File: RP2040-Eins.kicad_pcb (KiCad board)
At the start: 2 copper layers, 45 parts, among them J1 Barrel_Jack_Switch, J2 CONN_ICSP, J5 CONN_R3, J6 USB_B_Micro, J7 CONN_JTAG, Q1 AO3401A, SW1 BOOTSEL, SW2 RESET, U1 W25Q128JVS, U2 RP2040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

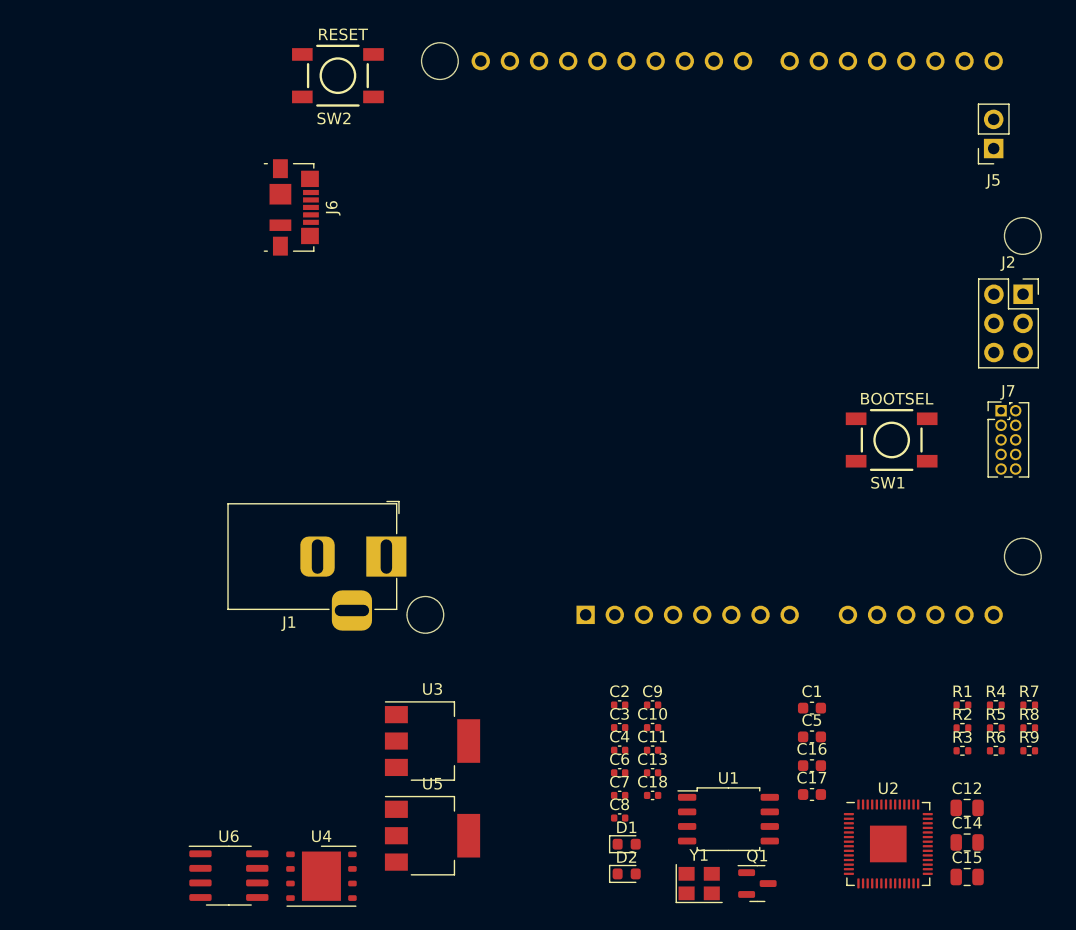
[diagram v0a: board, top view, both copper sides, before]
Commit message: Added board edge
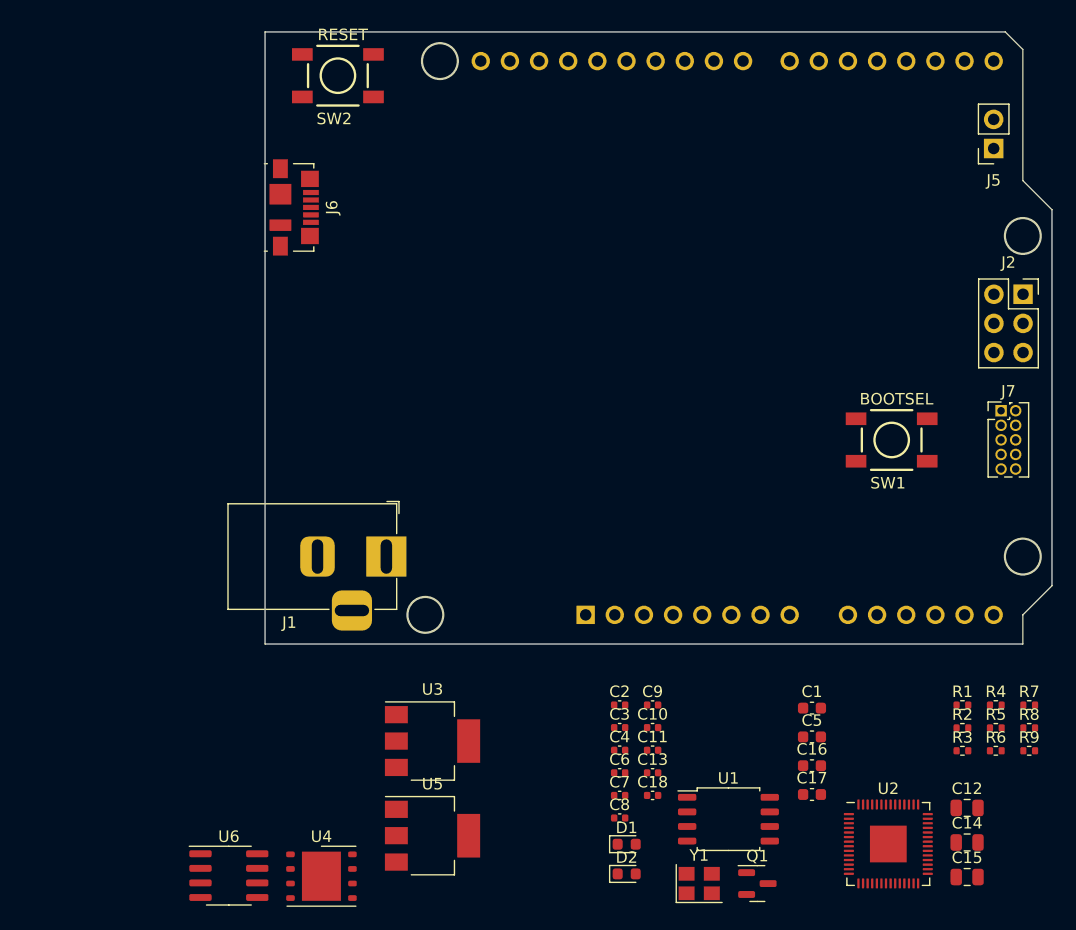
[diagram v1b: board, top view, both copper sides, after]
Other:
- board outline added: 68.6 x 53.3 mm
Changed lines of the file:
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@@
     )
   )
+  (gr_line (start 127 73.66) (end 191.516 73.66)
+    (stroke (width 0.1) (type default)) (layer "Edge.Cuts"))
+  (gr_line (start 193.04 75.184) (end 193.04 86.614)
+    (stroke (width 0.1) (type default)) (layer "Edge.Cuts"))
+  (gr_line (start 195.58 121.92) (end 193.04 124.46)
+    (stroke (width 0.1) (type default)) (layer "Edge.Cuts"))
+  (gr_line (start 191.516 73.66) (end 193.04 75.184)
+    (stroke (width 0.1) (type default)) (layer "Edge.Cuts"))
+  (gr_line (start 193.04 127) (end 127 127)
+    (stroke (width 0.1) (type default)) (layer "Edge.Cuts"))
+  (gr_line (start 193.04 86.614) (end 195.58 89.154)
+    (stroke (width 0.1) (type default)) (layer "Edge.Cuts"))
+  (gr_line (start 193.04 124.46) (end 193.04 127)
+    (stroke (width 0.1) (type default)) (layer "Edge.Cuts"))
+  (gr_circle (center 193.04 91.44) (end 193.04 89.916)
+    (stroke (width 0.1) (type default)) (fill none) (layer "Edge.Cuts"))
+  (gr_circle (center 193.04 119.38) (end 193.04 117.856)
+    (stroke (width 0.1) (type default)) (fill none) (layer "Edge.Cuts"))
+  (gr_line (start 127 127) (end 127 73.66)
+    (stroke (width 0.1) (type default)) (layer "Edge.Cuts"))
+  (gr_circle (center 142.24 76.2) (end 142.24 74.676)
+    (stroke (width 0.1) (type default)) (fill none) (layer "Edge.Cuts"))
+  (gr_line (start 195.58 89.154) (end 195.58 121.92)
+    (stroke (width 0.1) (type default)) (layer "Edge.Cuts"))
+  (gr_circle (center 140.97 124.46) (end 140.97 122.936)
+    (stroke (width 0.1) (type default)) (fill none) (layer "Edge.Cuts"))
 )

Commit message: Exchanged Arduino board shape with separate connectors
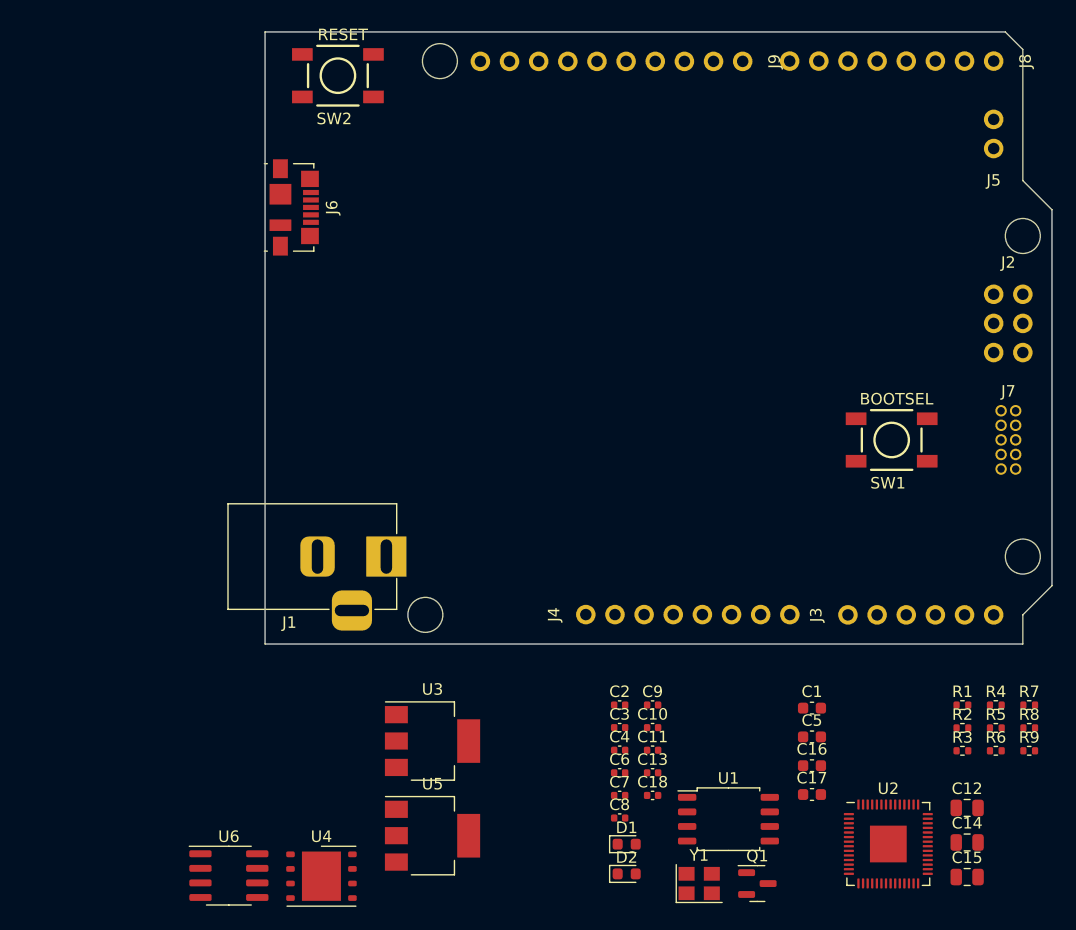
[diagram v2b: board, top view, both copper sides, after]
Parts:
- removed A1: Arduino_UNO_R3, Module:Arduino_UNO_R3_WithMountingHoles
- added J3: CONN_A, Connector_PinSocket_2.54mm:PinSocket_1x06_P2.54mm_Vertical, F.Cu at (177.8, 124.5)
- added J4: CONN_P, Connector_PinSocket_2.54mm:PinSocket_1x08_P2.54mm_Vertical, F.Cu at (155.0, 124.4)
- added J8: CONN_D1, Connector_PinSocket_2.54mm:PinSocket_1x08_P2.54mm_Vertical, F.Cu at (190.5, 76.2)
- added J9: CONN_D2, Connector_PinSocket_2.54mm:PinSocket_1x10_P2.54mm_Vertical, F.Cu at (168.6, 76.2)
- J2: value CONN_ICSP -> Conn_02x03_Odd_Even
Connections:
- J2 pad 1: D12_MISO -> +5V
- J2 pad 2: D13_SCK -> D12_MISO
- J2 pad 3: RESET -> D11_MOSI
- J2 pad 4: +5V -> D13_SCK
- J2 pad 5: D11_MOSI -> GND
- J2 pad 6: GND -> RESET

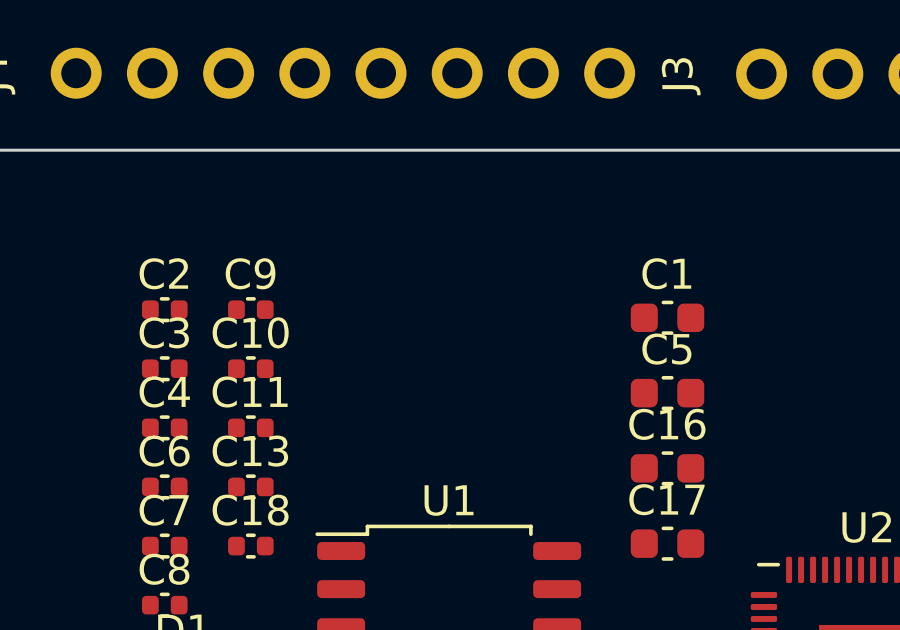
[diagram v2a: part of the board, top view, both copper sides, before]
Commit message: Added quartz caps. Moved stuff around.
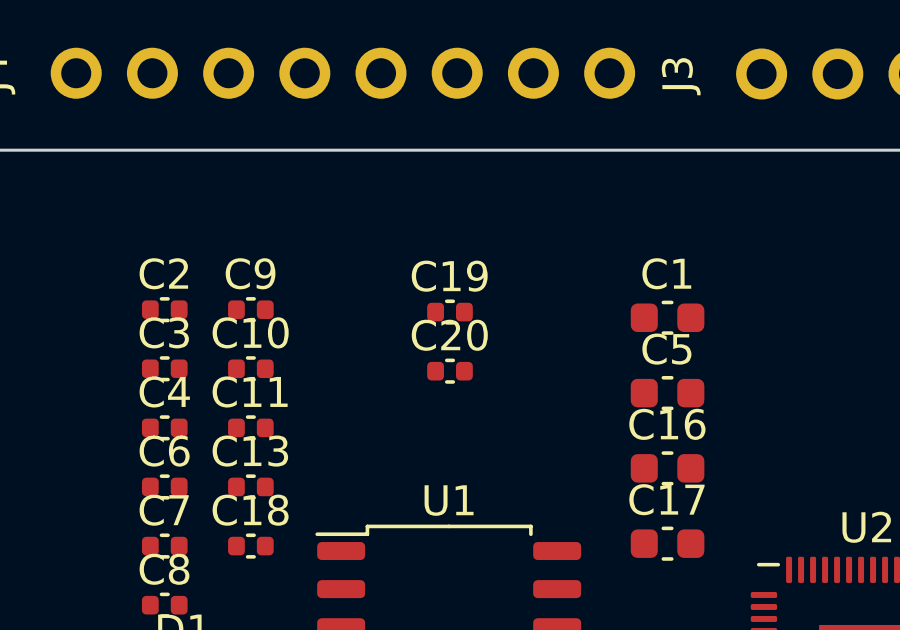
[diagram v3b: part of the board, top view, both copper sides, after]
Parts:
- added C19: 12pF, Capacitor_SMD:C_0402_1005Metric, F.Cu at (167.4, 132.4)
- added C20: 12pF, Capacitor_SMD:C_0402_1005Metric, F.Cu at (167.4, 134.4)
- J2: value Conn_02x03_Odd_Even -> CONN_I
- J5: value CONN_R3 -> CONN_X
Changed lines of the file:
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@@
+    )
+  )
+  (footprint "Capacitor_SMD:C_0402_1005Metric" (layer "F.Cu")
+    (at 167.414 134.366)
+    (descr "Capacitor SMD 0402 (1005 Metric), square (rectangular) end terminal, IPC_7351 nominal, (Body size source: IPC-SM-782 page 76, https://www.pcb-3d.com/wordpress/wp-content/uploads/ipc-sm-782a_amendment_1_and_2.pdf), generated with kicad-footprint-generator")
+    (tags "capacitor")
+    (property "Sheetfile" "RP2040-Eins.kicad_sch")
+    (property "Sheetname" "")
+    (property "ki_description" "Unpolarized capacitor, small symbol")
+    (property "ki_keywords" "capacitor cap")
+    (attr smd)
+    (fp_text reference "C20" (at 0 -1.16) (layer "F.SilkS")
+        (effects (font (size 1 1) (thickness 0.15)))
+    )
+    (fp_text value "12pF" (at 0 1.16) (layer "F.Fab")
+        (effects (font (size 1 1) (thickness 0.15)))
+    )
+    (fp_text user "${REFERENCE}" (at 0 0) (layer "F.Fab")
+        (effects (font (size 0.25 0.25) (thickness 0.04)))
+    )
+    (fp_line (start -0.107836 -0.36) (end 0.107836 -0.36)
+      (stroke (width 0.12) (type solid)) (layer "F.SilkS"))
+    (fp_line (start -0.107836 0.36) (end 0.107836 0.36)
+      (stroke (width 0.12) (type solid)) (layer "F.SilkS"))
+    (fp_line (start -0.91 -0.46) (end 0.91 -0.46)
+      (stroke (width 0.05) (type solid)) (layer "F.CrtYd"))
+    (fp_line (start -0.91 0.46) (end -0.91 -0.46)
+      (stroke (width 0.05) (type solid)) (layer "F.CrtYd"))
+    (fp_line (start 0.91 -0.46) (end 0.91 0.46)
+      (stroke (width 0.05) (type solid)) (layer "F.CrtYd"))
+    (fp_line (start 0.91 0.46) (end -0.91 0.46)
+      (stroke (width 0.05) (type solid)) (layer "F.CrtYd"))
+    (fp_line (start -0.5 -0.25) (end 0.5 -0.25)
+      (stroke (width 0.1) (type solid)) (layer "F.Fab"))
+    (fp_line (start -0.5 0.25) (end -0.5 -0.25)
+      (stroke (width 0.1) (type solid)) (layer "F.Fab"))
+    (fp_line (start 0.5 -0.25) (end 0.5 0.25)
+      (stroke (width 0.1) (type solid)) (layer "F.Fab"))
+    (fp_line (start 0.5 0.25) (end -0.5 0.25)
+      (stroke (width 0.1) (type solid)) (layer "F.Fab"))
+    (pad "1" smd roundrect (at -0.48 0) (size 0.56 0.62) (layers "F.Cu" "F.Paste" "F.Mask") (roundrect_rratio 0.25)
+      (net 59 "XOUT") (pintype "passive"))
+    (pad "2" smd roundrect (at 0.48 0) (size 0.56 0.62) (layers "F.Cu" "F.Paste" "F.Mask") (roundrect_rratio 0.25)
+      (net 4 "GND") (pintype "passive"))
+    (model "${KICAD6_3DMODEL_DIR}/Capacitor_SMD.3dshapes/C_0402_1005Metric.wrl"
+      (offset (xyz 0 0 0))
+      (scale (xyz 1 1 1))
+      (rotate (xyz 0 0 0))
     )
   )
@@
     )
   )
+  (footprint "Capacitor_SMD:C_0402_1005Metric" (layer "F.Cu")
+    (at 167.414 132.396)
+    (descr "Capacitor SMD 0402 (1005 Metric), square (rectangular) end terminal, IPC_7351 nominal, (Body size source: IPC-SM-782 page 76, https://www.pcb-3d.com/wordpress/wp-content/uploads/ipc-sm-782a_amendment_1_and_2.pdf), generated with kicad-footprint-generator")
+    (tags "capacitor")
+    (property "Sheetfile" "RP2040-Eins.kicad_sch")
+    (property "Sheetname" "")
+    (property "ki_description" "Unpolarized capacitor, small symbol")
+    (property "ki_keywords" "capacitor cap")
+    (attr smd)
+    (fp_text reference "C19" (at 0 -1.16) (layer "F.SilkS")
+        (effects (font (size 1 1) (thickness 0.15)))
+    )
+    (fp_text value "12pF" (at 0 1.16) (layer "F.Fab")
+        (effects (font (size 1 1) (thickness 0.15)))
+    )
+    (fp_text user "${REFERENCE}" (at 0 0) (layer "F.Fab")
+        (effects (font (size 0.25 0.25) (thickness 0.04)))
+    )
+    (fp_line (start -0.107836 -0.36) (end 0.107836 -0.36)
+      (stroke (width 0.12) (type solid)) (layer "F.SilkS"))
+    (fp_line (start -0.107836 0.36) (end 0.107836 0.36)
+      (stroke (width 0.12) (type solid)) (layer "F.SilkS"))
+    (fp_line (start -0.91 -0.46) (end 0.91 -0.46)
+      (stroke (width 0.05) (type solid)) (layer "F.CrtYd"))
+    (fp_line (start -0.91 0.46) (end -0.91 -0.46)
+      (stroke (width 0.05) (type solid)) (layer "F.CrtYd"))
+    (fp_line (start 0.91 -0.46) (end 0.91 0.46)
+      (stroke (width 0.05) (type solid)) (layer "F.CrtYd"))
+    (fp_line (start 0.91 0.46) (end -0.91 0.46)
+      (stroke (width 0.05) (type solid)) (layer "F.CrtYd"))
+    (fp_line (start -0.5 -0.25) (end 0.5 -0.25)
+      (stroke (width 0.1) (type solid)) (layer "F.Fab"))
+    (fp_line (start -0.5 0.25) (end -0.5 -0.25)
+      (stroke (width 0.1) (type solid)) (layer "F.Fab"))
+    (fp_line (start 0.5 -0.25) (end 0.5 0.25)
+      (stroke (width 0.1) (type solid)) (layer "F.Fab"))
+    (fp_line (start 0.5 0.25) (end -0.5 0.25)
+      (stroke (width 0.1) (type solid)) (layer "F.Fab"))
+    (pad "1" smd roundrect (at -0.48 0) (size 0.56 0.62) (layers "F.Cu" "F.Paste" "F.Mask") (roundrect_rratio 0.25)
+      (net 58 "XIN") (pintype "passive"))
+    (pad "2" smd roundrect (at 0.48 0) (size 0.56 0.62) (layers "F.Cu" "F.Paste" "F.Mask") (roundrect_rratio 0.25)
+      (net 4 "GND") (pintype "passive"))
+    (model "${KICAD6_3DMODEL_DIR}/Capacitor_SMD.3dshapes/C_0402_1005Metric.wrl"
+      (offset (xyz 0 0 0))
+      (scale (xyz 1 1 1))
+      (rotate (xyz 0 0 0))
+    )
+  )
   (footprint "Resistor_SMD:R_0402_1005Metric" (layer "F.Cu")
     (at 190.686 132.326)
@@
         (effects (font (size 1 1) (thickness 0.15)))
     )
-    (fp_text value "Conn_02x03_Odd_Even" (at -1.27 7.85) (layer "F.Fab")
+    (fp_text value "CONN_I" (at -1.27 7.85) (layer "F.Fab")
         (effects (font (size 1 1) (thickness 0.15)))
     )
@@
         (effects (font (size 1 1) (thickness 0.15)))
     )
-    (fp_text value "CONN_R3" (at 0 5.31 180) (layer "F.Fab")
-        (effects (font (size 1 1) (thickness 0.15)))
-    )
+    (fp_text value "CONN_X" (at 0 5.31 180) (layer "F.Fab")
+        (effects (font (size 1 1) (thickness 0.15)))
+    )

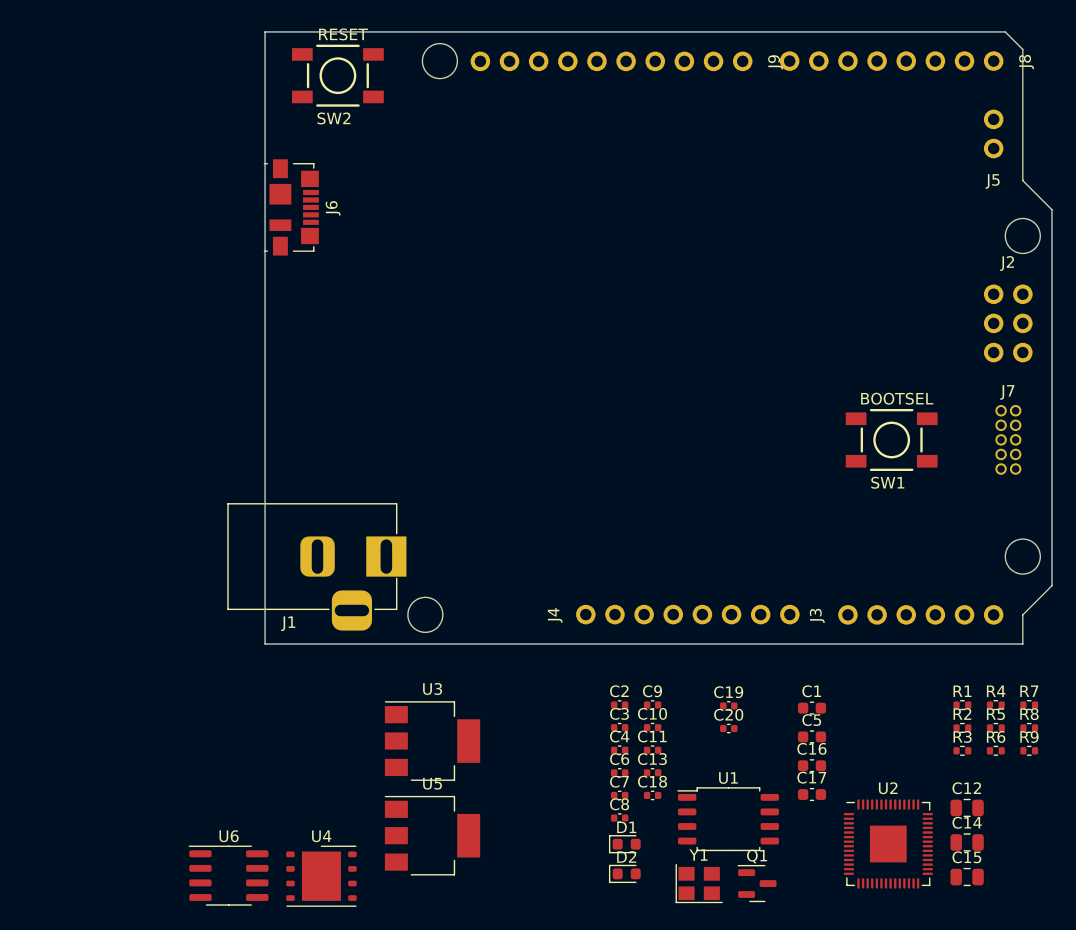
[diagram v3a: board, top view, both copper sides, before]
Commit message: Switched to USB-C with all stuff around it.
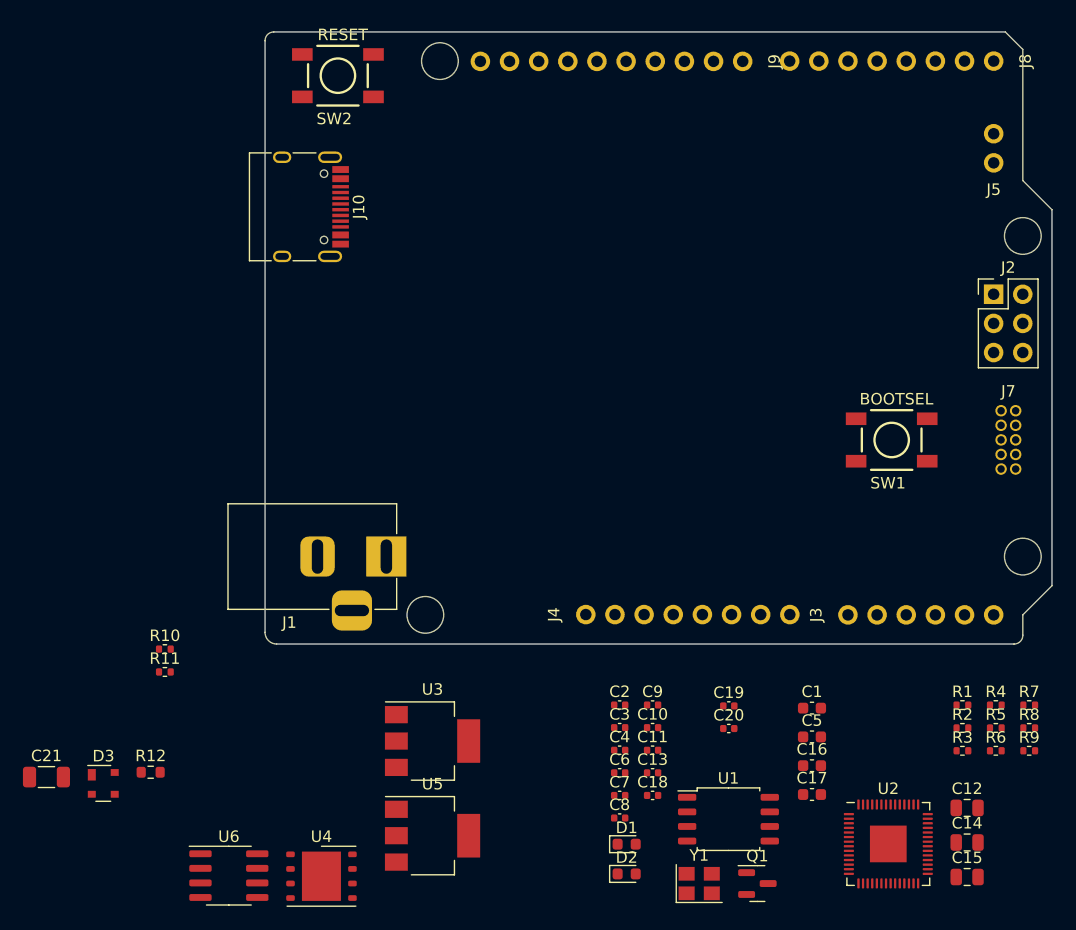
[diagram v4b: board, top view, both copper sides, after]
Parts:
- removed J6: USB_B_Micro, Connector_USB:USB_Micro-B_Molex_47346-0001
- added C21: 4.7nF 1kV, Capacitor_SMD:C_1206_3216Metric, F.Cu at (108.0, 138.6)
- added D3: PRTR5V0U2X, Package_TO_SOT_SMD:SOT-143, F.Cu at (112.9, 139.1)
- added J10: USB_C_Receptacle_USB2.0, Connector_USB:USB_C_Receptacle_HRO_TYPE-C-31-M-12, F.Cu at (129.5, 88.9)
- added R10: 5k1, Resistor_SMD:R_0402_1005Metric, F.Cu at (118.3, 127.4)
- added R11: 5k1, Resistor_SMD:R_0402_1005Metric, F.Cu at (118.3, 129.4)
- added R12: 1M, Resistor_SMD:R_0603_1608Metric, F.Cu at (117.0, 138.2)
- J2: footprint Connector_PinSocket_2.54mm:PinSocket_2x03_P2.54mm_Vertical -> Connector_PinHeader_2.54mm:PinHeader_2x03_P2.54mm_Vertical
- J5: footprint Connector_PinSocket_2.54mm:PinSocket_1x02_P2.54mm_Vertical -> Connector_PinHeader_2.54mm:PinHeader_1x02_P2.54mm_Vertical
- moved J2 2.54 mm to (190.5, 96.5)
- moved J5 1.25 mm to (190.5, 85.1)
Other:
- outline, holes or cut-outs redrawn
